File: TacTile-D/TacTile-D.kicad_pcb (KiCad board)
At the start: 2 copper layers, 60 x 60 mm, 17 parts, among them J1 Conn_01x06, J2 Conn_01x06, J3 Conn_01x06, J4 Conn_01x06, J5 Conn_01x04, J6 Conn_01x05, J7 Conn_01x02, J8 Conn_01x02, U1 74LS04, U2 4011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

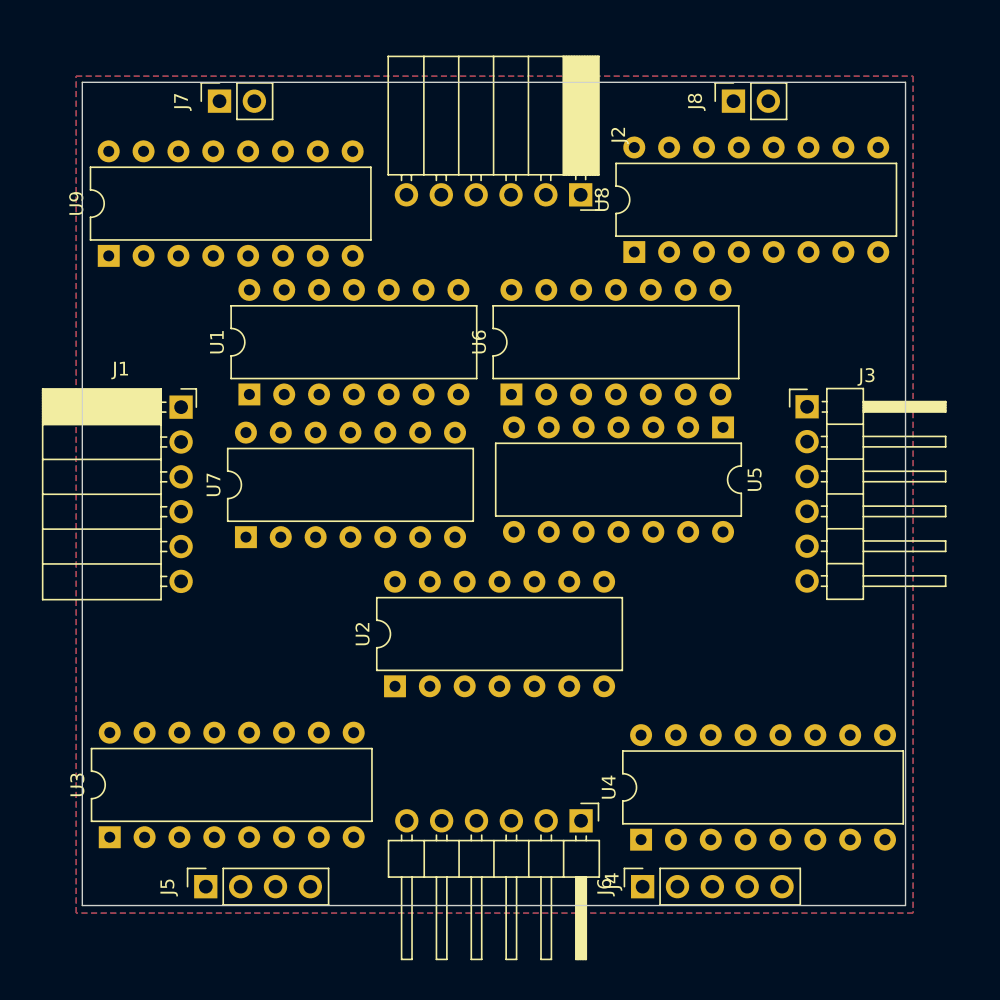
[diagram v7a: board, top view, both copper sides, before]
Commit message: Finished layout with new ICs on board D
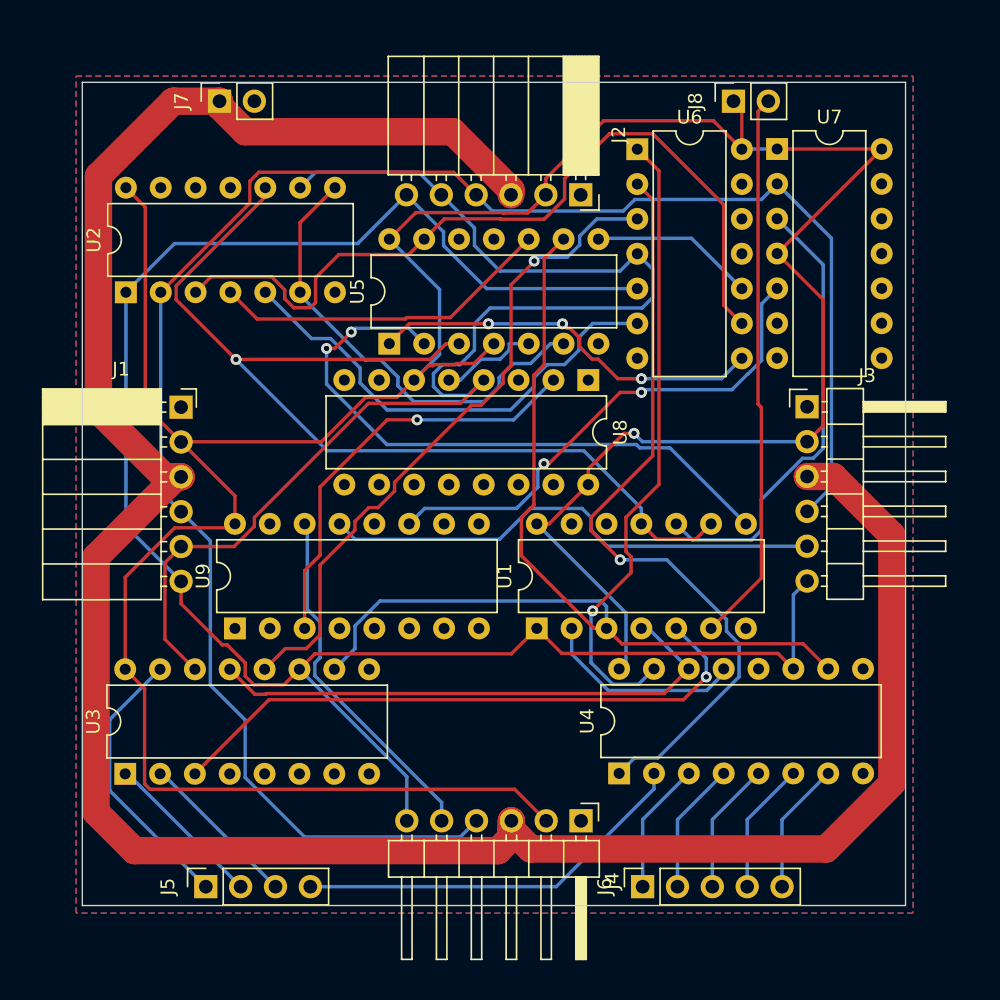
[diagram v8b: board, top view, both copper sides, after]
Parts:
- moved U7 47.9 mm to (75.6, 29.9), turned to 0 degrees
- moved U2 34.8 mm to (28.2, 40.3)
- moved U9 28.7 mm to (36.1, 64.8)
- moved U1 27.0 mm to (58.1, 64.8)
- moved U5 25.1 mm to (47.4, 44.0), turned to 90 degrees
- moved U6 20.1 mm to (65.5, 29.9), turned to 0 degrees
- moved U8 9.91 mm to (61.9, 46.7), turned to -90 degrees
- moved U4 5.09 mm to (64.1, 75.4)
- moved U3 4.75 mm to (28.1, 75.4)
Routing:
- net VCC: track 0.00 -> 229.9 mm, vias 0 -> 1
- net VIN: track 0.00 -> 177.9 mm
- net CLK: track 0.00 -> 139.6 mm
- net SS: track 0.00 -> 134.8 mm
- net MOSI: track 0.00 -> 95.5 mm
- net Net-(U5A-C): track 0.00 -> 74.9 mm, vias 0 -> 1
- net SEN: track 0.00 -> 74.8 mm
- net Net-(U5B-~{R}): track 0.00 -> 58.8 mm
- net Net-(U4-Q1): track 0.00 -> 56.4 mm, vias 0 -> 1
- net Net-(U3-RCLK): track 0.00 -> 48.8 mm, vias 0 -> 1
- net Net-(U4-Q0): track 0.00 -> 46.1 mm, vias 0 -> 1
- net Net-(U5A-D): track 0.00 -> 45.6 mm, vias 0 -> 2
- net Net-(U3-QD): track 0.00 -> 44.6 mm, vias 0 -> 1
- net LEN: track 0.00 -> 40.4 mm
- net Net-(U3-~{OE}): track 0.00 -> 39.7 mm
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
